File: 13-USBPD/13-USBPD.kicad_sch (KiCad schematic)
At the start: 29 parts, among them J1 USB_C_Receptacle, U1 STUSB4500QTR

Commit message: Day 14 - layout progress on USBPD
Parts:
- removed R? (x2): DNP, symbol Device:R_Small_US
- added J2: Conn_01x02_Female, symbol Connector:Conn_01x02_Female
- added TP1, TP2, TP3, TP4, TP5, TP6, TP7: TestPoint, TestPoint:TestPoint_Pad_D1.0mm, symbol Connector:TestPoint
- C1, C2, C3, C4, C5, C6: renamed from C?; footprint (none) -> Capacitor_SMD:C_0402_1005Metric_Pad0.74x0.62mm_HandSolder
- D1: renamed from D?; footprint (none) -> Package_TO_SOT_SMD:SOT-323_SC-70_Handsoldering
- D3: renamed from D?; value LED_Small -> RED; footprint (none) -> LED_SMD:LED_0402_1005Metric_Pad0.77x0.64mm_HandSolder
- D4: renamed from D?; value LED_Small -> GRN; footprint (none) -> LED_SMD:LED_0402_1005Metric_Pad0.77x0.64mm_HandSolder
- D5: renamed from D?; value LED_Small -> BLU; footprint (none) -> LED_SMD:LED_0402_1005Metric_Pad0.77x0.64mm_HandSolder
- D6: renamed from D?; footprint (none) -> Diode_SMD:D_SMA-SMB_Universal_Handsoldering
- R10, R2, R3, R4, R6, R7, R8, R9: renamed from R?; footprint (none) -> Resistor_SMD:R_0402_1005Metric_Pad0.72x0.64mm_HandSolder
- gave numbers to parts that had none: 6
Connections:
- net ADDR0: now also TP6.1
- net ADDR1: now also TP7.1
- net GND: now also C6.2, R12.2, J2.2 (Pin_2)
- net VBUS: now also D3.2 (A), D4.2 (A), D5.2 (A)
- net VOUT: now also J2.1 (Pin_1)
- net at Q1.4, R12.1, R9.2: now also R10.2; no longer R10.1
- net at U1.11 (ATTACH): now also TP5.1
- net at U1.16 (VBUS_EN_SNK): now also R10.1; no longer R10.2
- net at U1.17 (A_B_SIDE): now also TP4.1
- net at U1.19 (ALERT): now also TP3.1
- net at U1.7 (SCL): now also TP1.1
- net at U1.8 (SDA): now also TP2.1
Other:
- moved on the sheet: C6, D3, D5, D6, Q1, R10, R11, R12, R14, R2, R6, R9

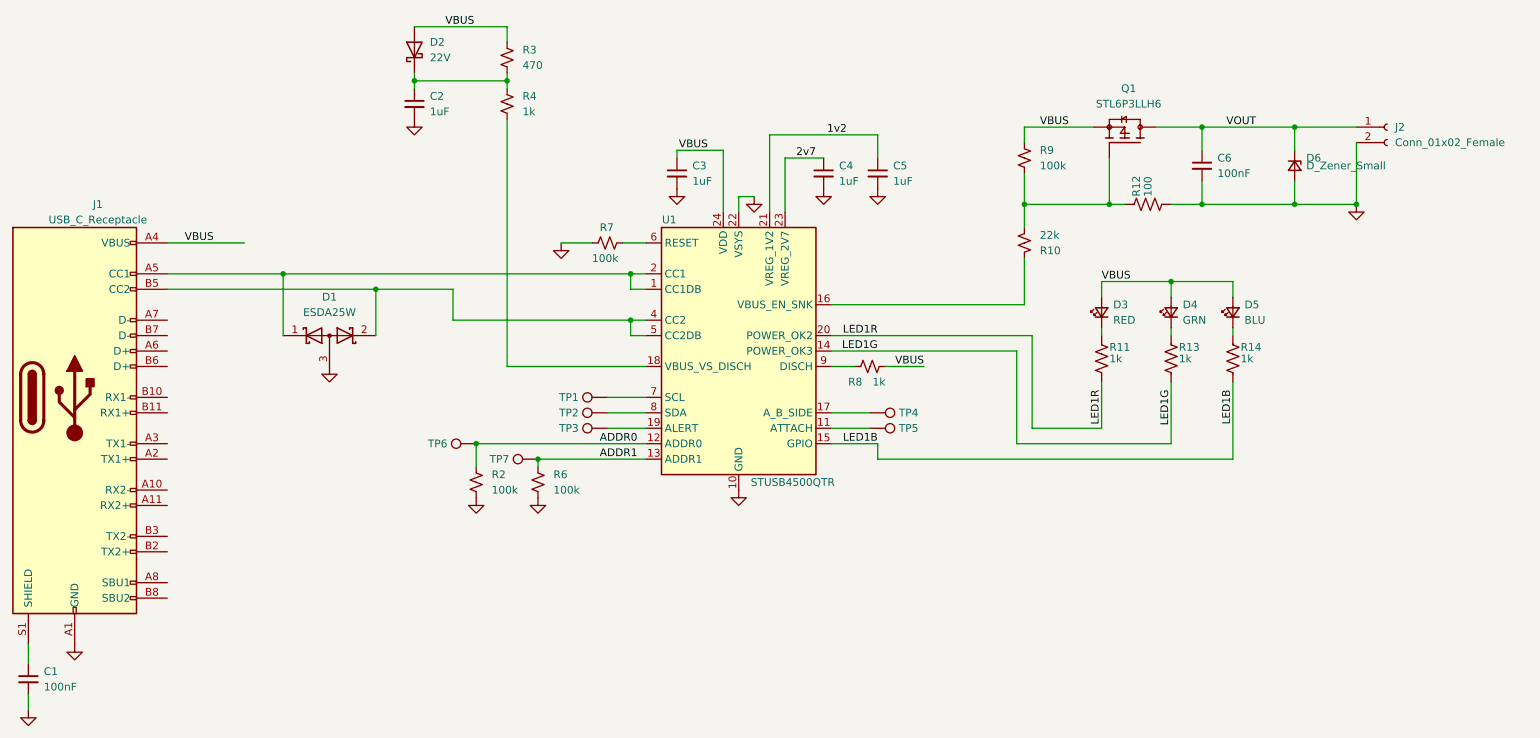
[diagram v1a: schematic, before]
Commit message: Day 15: Add powerpole outputs, test points, check SCH. Needs some DRC love, mostly courtyard of testpoint violations at the moments.
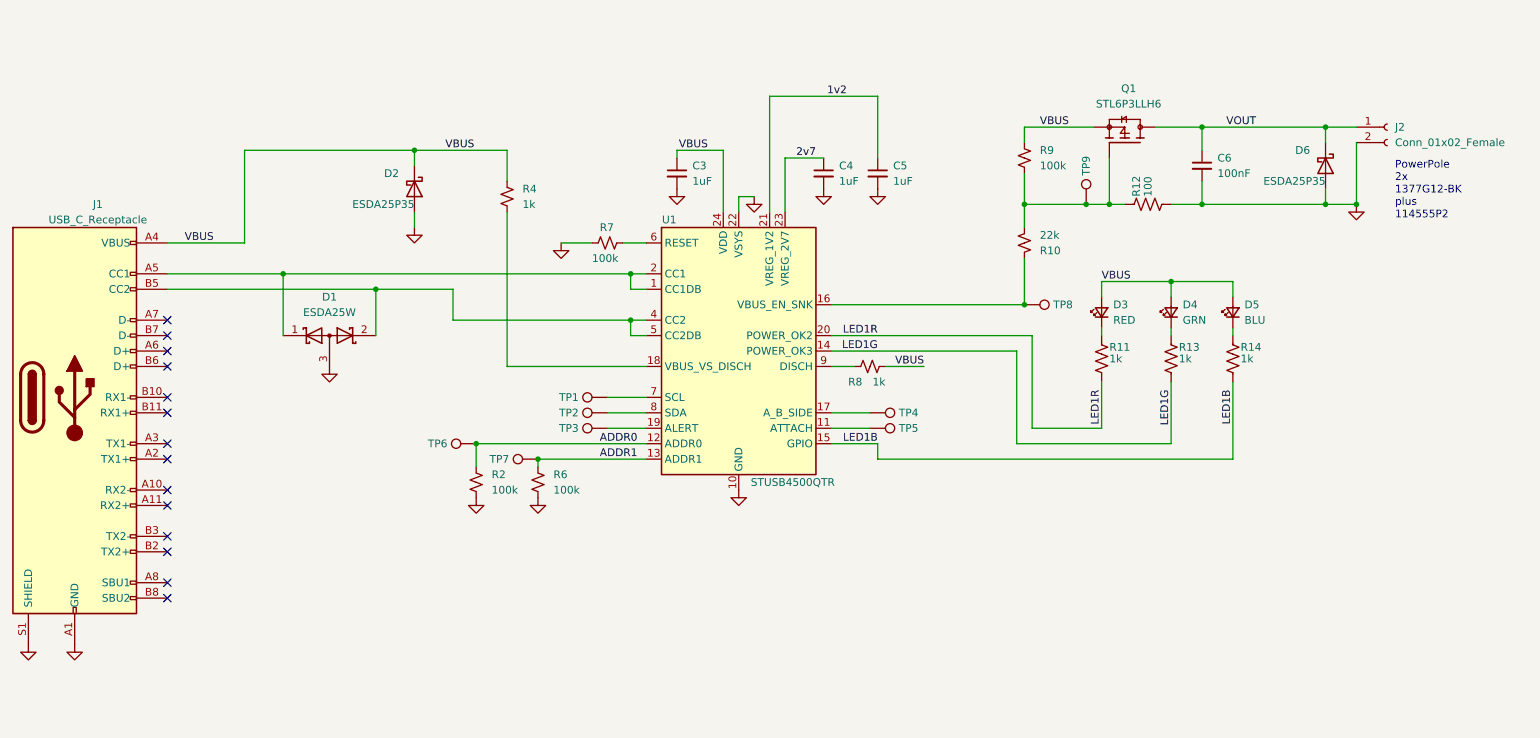
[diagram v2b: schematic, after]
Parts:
- removed C1: 100nF, Capacitor_SMD:C_0402_1005Metric_Pad0.74x0.62mm_HandSolder, symbol Device:C_Small
- removed C2: 1uF, Capacitor_SMD:C_0402_1005Metric_Pad0.74x0.62mm_HandSolder, symbol Device:C_Small
- removed D6: D_Zener_Small, Diode_SMD:D_SMA-SMB_Universal_Handsoldering, symbol Device:D_Zener_Small
- removed R3: 470, Resistor_SMD:R_0402_1005Metric_Pad0.72x0.64mm_HandSolder, symbol Device:R_Small_US
- added D6: ESDA25P35, 13-USBPD:DIODE_SMD_1610, symbol Device:D_Schottky
- added TP8, TP9: TestPoint, TestPoint:TestPoint_Pad_D1.0mm, symbol Connector:TestPoint
- D2: value 22V -> ESDA25P35; footprint Diode_SMD:D_SMA-SMB_Universal_Handsoldering -> 13-USBPD:DIODE_SMD_1610
- J2: footprint (none) -> 13-USBPD:PowerPole_Horizontal_1x2_with_staple
- R4: footprint Resistor_SMD:R_0402_1005Metric_Pad0.72x0.64mm_HandSolder -> Resistor_SMD:R_0805_2012Metric_Pad1.20x1.40mm_HandSolder
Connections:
- net GND: now also D2.2 (A), J1.S1 (SHIELD), D6.2 (A)
- net VBUS: now also D2.1 (K), R4.1; no longer D2.2 (A)
- net VOUT: now also D6.1 (K)
- net at Q1.4, R10.2, R12.1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: now also TP9.1
- net at R10.1, U1.16 (VBUS_EN_SNK): now also TP8.1
- no-connect marks 0 -> 14
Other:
- note added: "PowerPole 2x 1377G12-BK plus 114555P2"
- moved on the sheet: R4
